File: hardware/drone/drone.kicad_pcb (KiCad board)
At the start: 6 copper layers, 45 x 45 mm, 246 parts, among them J1 54548-2272, J2 BM08B-SRSS-TB_LF__SN_, J3 USB_C_Receptacle_USB2.0_16P, J4 Conn_ARM_SWD_TagConnect_TC2030, J5 Conn_01x06_Pin, J6 Conn_01x02_Socket, Q1 ISP650P06NM, SW1 SW_MEC_5E, U1 STM32N645I0, U10 PE4259, U11 TAC5111IRGER, U12 LP5907, U14 ICM-42688-P, U15 SAM_M10Q, U16 LMR51635XFDDCR, U17 TXU0204, U18 TPS2121, U19 BMP581, U2 SX1262IMLTRT, U20 TVS0500DRV, U21 TCA9406DC, U22 LIS2MDL, U23 MM8030_2610RJ3, U24 MM8030_2610RJ3, U25 ECMF2-40A100N6, U26 ECMF2-40A100N6, U27 ECMF2-40A100N6, U28 LM4670ITL/NOPB, U3 TPS628303, U4 TPS7A2118PQWDSGRQ1, U5 TPS628303, U6 MX25UW25645GXDI00, U7 CC3350, U8 DPX167125DT-8197B1, U9 DEA162450BT-1295A1, Y1 Crystal_GND24, Y2 Crystal_GND24, Y3 Crystal_GND24, Y4 Crystal

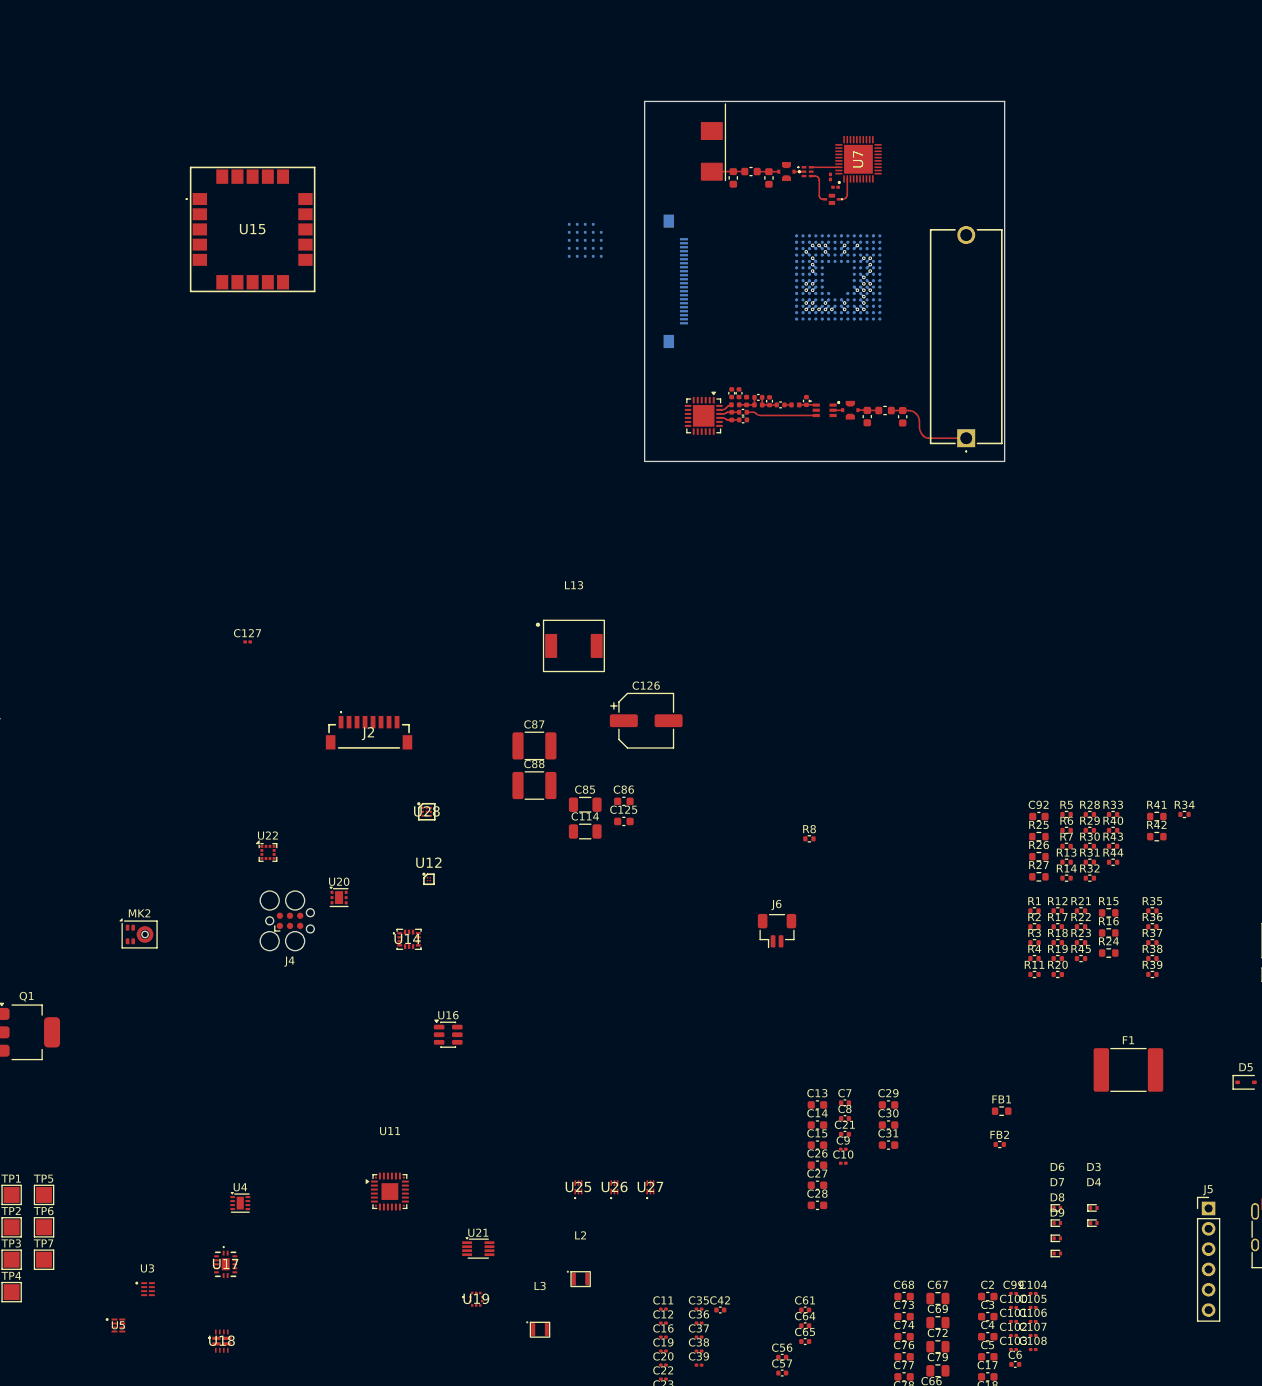
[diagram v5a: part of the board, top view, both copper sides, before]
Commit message: Placed SMPS layouts and optimized for space
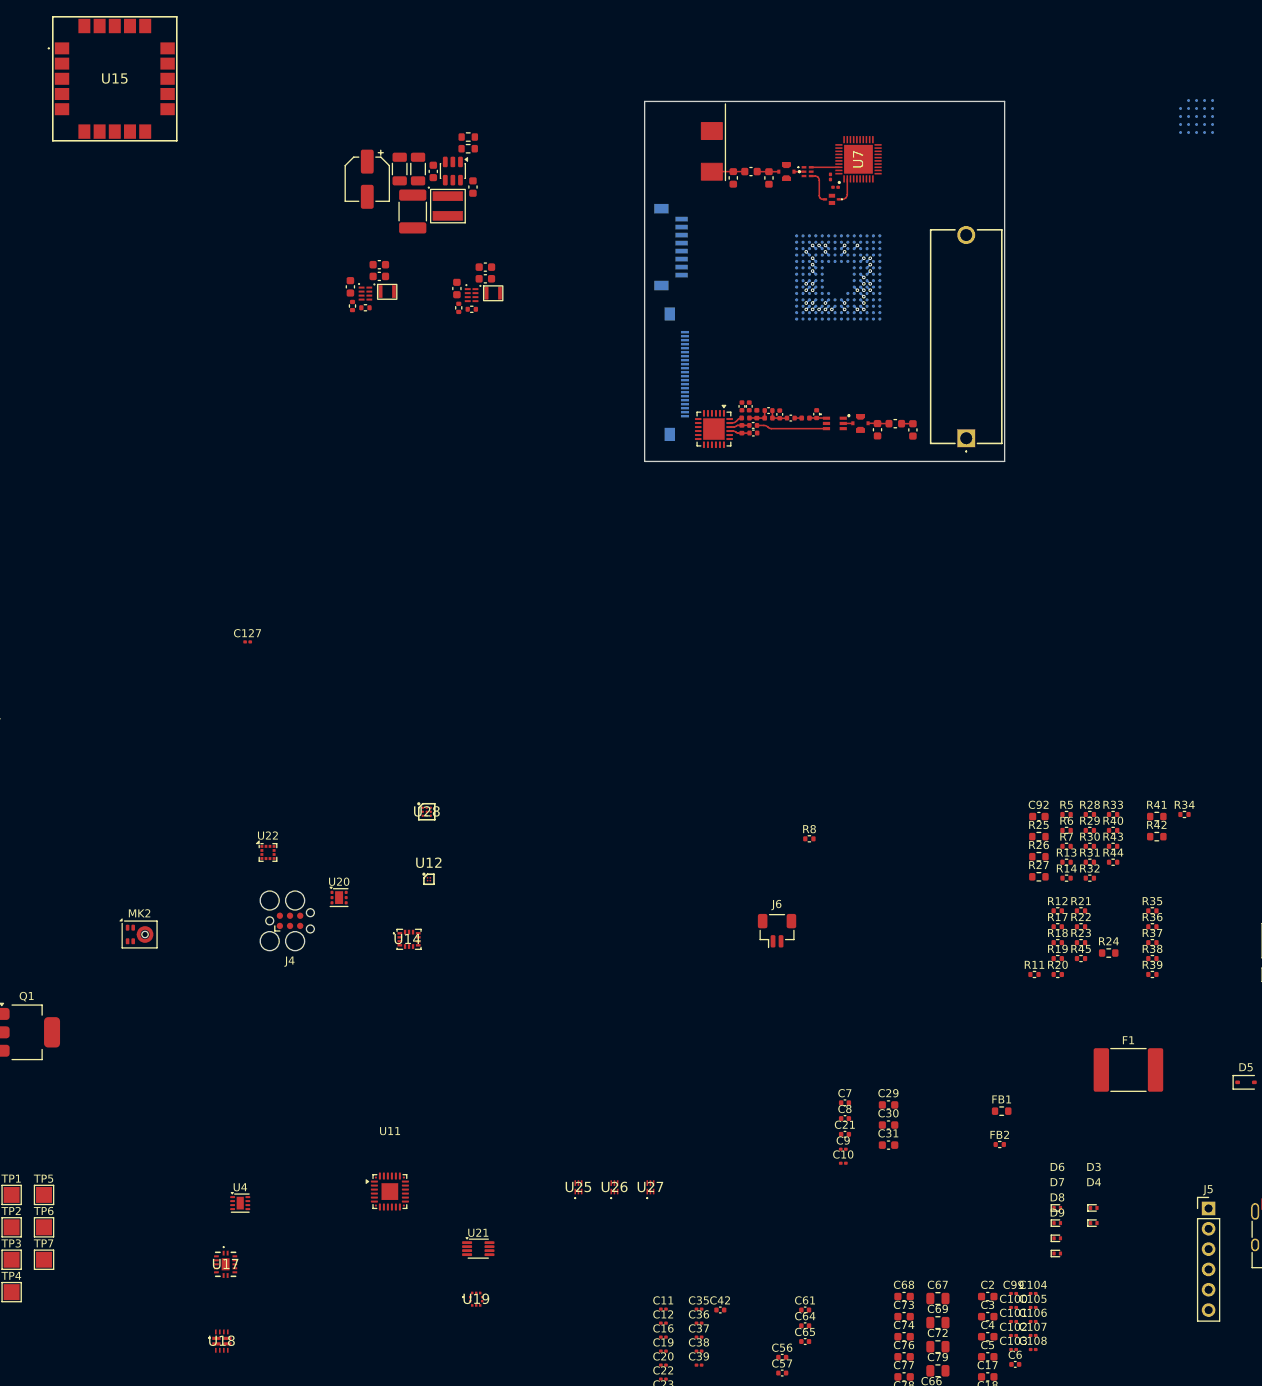
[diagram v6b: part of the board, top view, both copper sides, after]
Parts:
- removed C87: 33u, Capacitor_SMD:C_1812_4532Metric
- C126: value 22u -> 10u; footprint Capacitor_SMD:CP_Elec_6.3x5.4 -> Capacitor_SMD:CP_Elec_5x5.4
- J2: moved to B.Cu
- L13: value 10u -> 3.3u; footprint SoftDroneLibrary:CYA0650-10UH -> SoftDroneLibrary:74439324033
- U16: value LMR51635XFDDCR -> LMR51635YFDDCR
- moved U5 136.2 mm to (149.4, 111.2)
- moved L3 129.7 mm to (152.1, 111.0)
- moved U3 127.4 mm to (136.1, 111.0)
- moved R16 126.6 mm to (148.9, 92.9)
- moved R15 125.8 mm to (148.9, 91.5), turned to 180 degrees
- moved L2 125.8 mm to (138.8, 110.8)
- moved C28 124.4 mm to (151.1, 107.7), turned to 180 degrees
- moved C15 121.6 mm to (137.8, 108.9), turned to 180 degrees
- moved C14 120.7 mm to (137.8, 107.4), turned to 180 degrees
- moved C27 120.7 mm to (151.1, 109.2), turned to 180 degrees
- moved C26 118.5 mm to (147.5, 110.4), turned to -90 degrees
- moved C13 117.8 mm to (134.2, 110.2), turned to -90 degrees
- moved R2 115.3 mm to (134.5, 112.6), turned to 90 degrees
- moved R1 112.6 mm to (136.1, 112.8), turned to 180 degrees
- moved R4 108.6 mm to (147.8, 112.8), turned to 90 degrees
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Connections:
- net Net-(U16-CB) renamed /Power/VSYS_5V_CB
- net Net-(U3-PG) renamed /Power/VDD1V8_PG
- net Net-(U5-PG) renamed /Power/VDD3V3_PG
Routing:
- net /RF_915/RFCSUBG_ANT: track 11.6 -> 1.42 mm

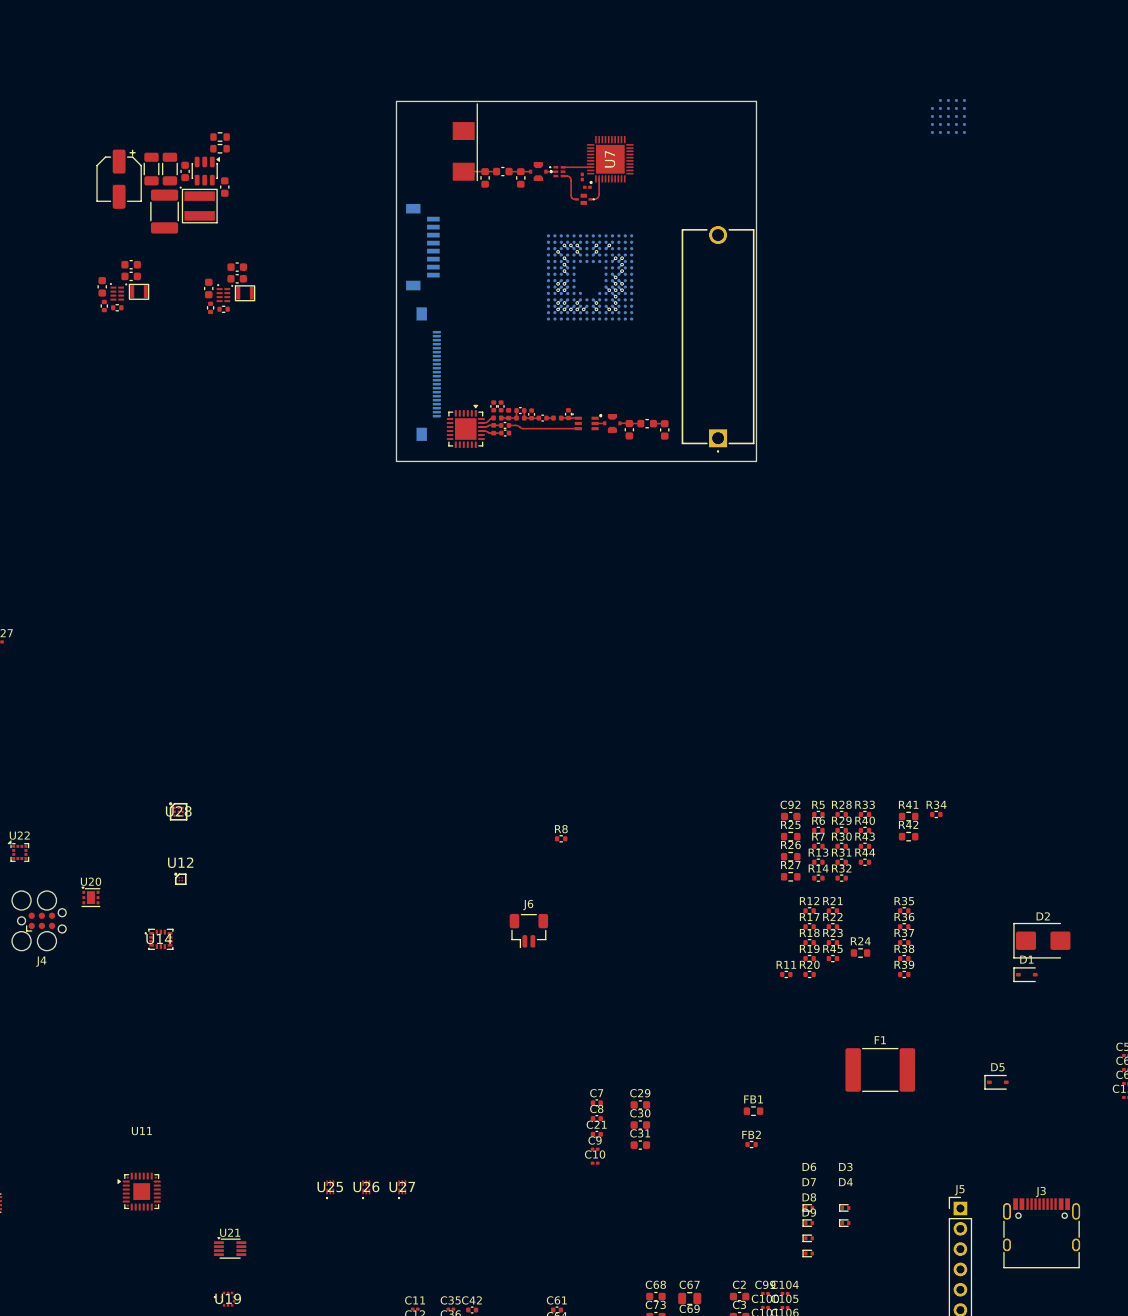
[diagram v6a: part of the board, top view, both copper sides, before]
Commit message: Fixed 3D model of antenna
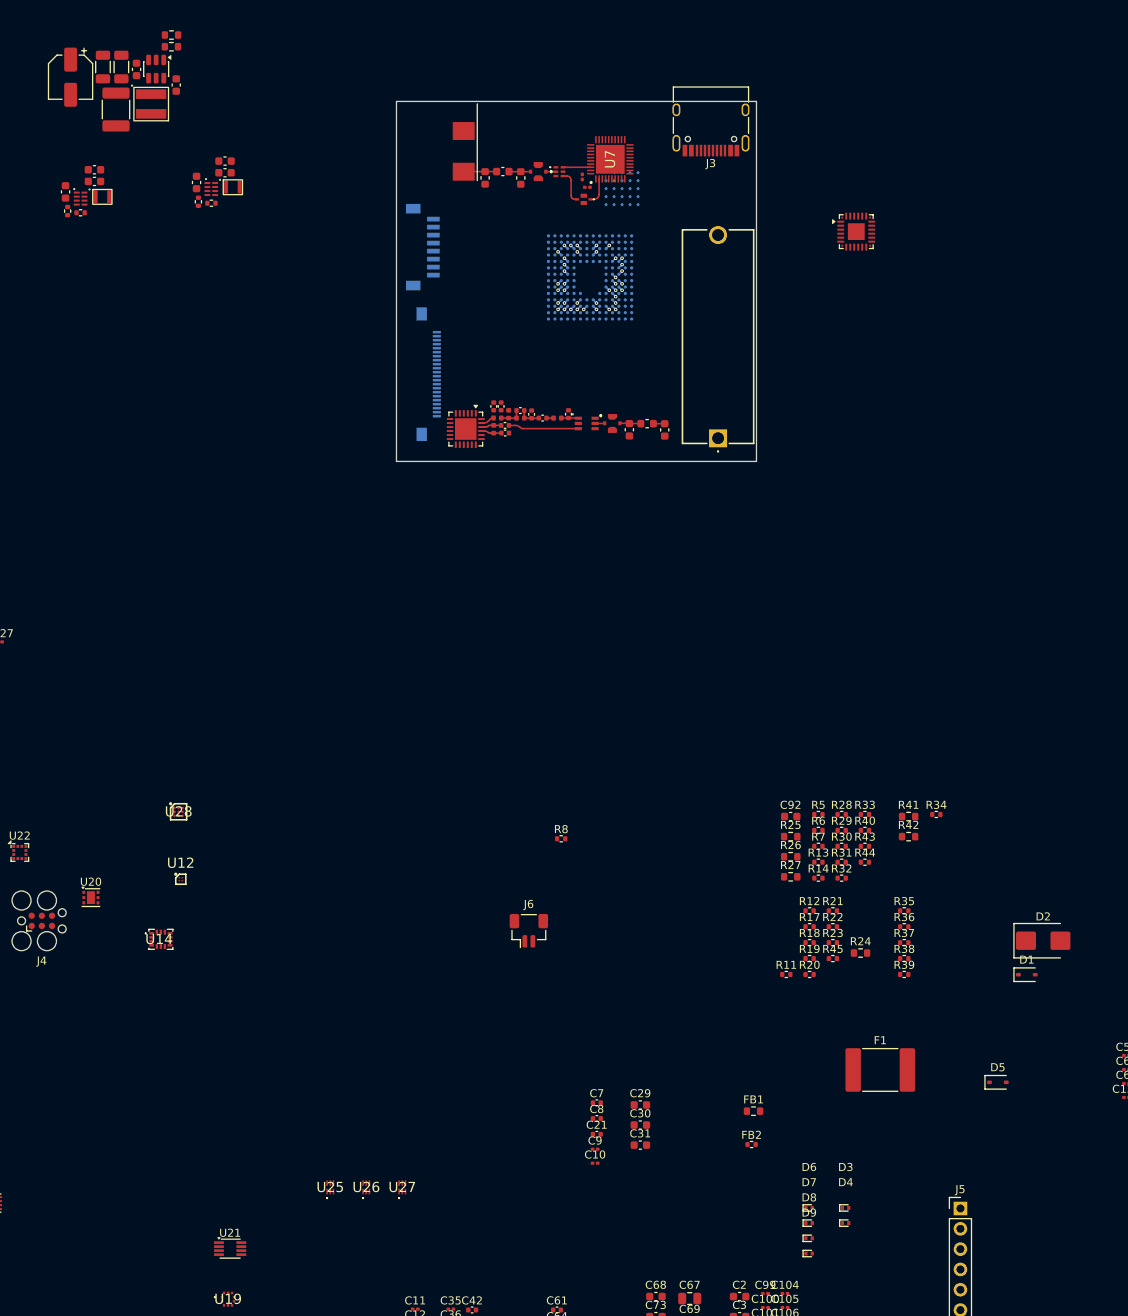
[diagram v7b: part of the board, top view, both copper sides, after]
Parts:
- moved U11 149.6 mm to (228.5, 103.2)
- moved J3 145.8 mm to (210.3, 89.1), turned to 180 degrees
- moved U6 41.8 mm to (199.2, 97.9)
- moved C125 14.1 mm to (138.5, 83.0)
- moved C126 14.1 mm to (130.3, 84.0)
- moved C114 14.1 mm to (136.6, 82.7)
- moved C85 14.1 mm to (134.3, 82.7)
- moved C86 14.1 mm to (143.5, 85.0)
- moved C88 14.1 mm to (135.9, 88.0)
- moved L13 14.1 mm to (140.3, 87.3)
- moved R15 14.1 mm to (142.9, 78.7)
- moved R16 14.1 mm to (142.9, 80.2)
- moved U16 14.1 mm to (141.0, 83.0)
- moved C26 13.3 mm to (146.0, 97.1)
- moved R3 13.3 mm to (147.9, 99.7)
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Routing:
- added copper zone on In1.Cu, net GND
- added copper zone on In4.Cu, net GND

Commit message: Routed OSPI
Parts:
- removed C126: 10u, Capacitor_SMD:CP_Elec_5x5.4
- removed Q1: ISP650P06NM, Package_TO_SOT_SMD:SOT-223
- added U13: SQA411CEJW-T1_GE3, SQA411CEJW-T1_GE3:SQA411CEJWT1_GE3, B.Cu at (203.2, 95.5)
- C114, C125, C13, C14, C15, C26, C27, C28, C29, C30, C31, C32, C33, C34, C85, C86, C88, D1, J3, L13, L2, L3, R1, R15, R16, R2, R3, R4, U11, U16, U18, U3, U5: moved to B.Cu
- F1: value 2920L150/60MR -> SF-0603SP200R-2; footprint Fuse:Fuse_2920_7451Metric -> Fuse:Fuse_0603_1608Metric; moved to B.Cu
- J1, U6: moved to F.Cu
- U25, U26, U27: footprint ECMF2-40A100N6:ECMF240A100N6 -> SoftDroneLibrary:ECMF2-40A100N6
- moved U18 183.5 mm to (219.6, 89.0), turned to 90 degrees
- moved C34 144.7 mm to (195.2, 109.5), turned to 180 degrees
- moved C33 138.8 mm to (196.0, 113.5)
- moved C32 138.8 mm to (199.5, 111.9), turned to -90 degrees
- moved U25 132.0 mm to (196.8, 95.2), turned to 180 degrees
- moved U26 131.8 mm to (200.6, 95.2), turned to 180 degrees
- moved U27 130.4 mm to (198.7, 95.2), turned to 180 degrees
- moved F1 118.9 mm to (200.9, 93.1)
- moved D1 111.7 mm to (201.2, 95.5), turned to -90 degrees
- moved C31 109.4 mm to (195.2, 108.3), turned to 180 degrees
- moved C29 100.6 mm to (200.7, 111.9), turned to -90 degrees
- moved C30 100.4 mm to (196.0, 114.7)
- moved C26 83.4 mm to (229.2, 103.3)
- moved R4 82.9 mm to (228.9, 105.7)
- moved U5 79.7 mm to (227.3, 104.1), turned to 180 degrees
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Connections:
- net /Camera/CSI_CKN_CON renamed /Camera/CSI_CON_CKN
- net /Camera/CSI_CKP_CON renamed /Camera/CSI_CON_CKP
- net /Camera/CSI_D0N_CON renamed /Camera/CSI_CON_D0N
- net /Camera/CSI_D0P_CON renamed /Camera/CSI_CON_D0P
- net /Camera/CSI_D1N_CON renamed /Camera/CSI_CON_D1N
- net /Camera/CSI_D1P_CON renamed /Camera/CSI_CON_D1P
- net Net-(U2-DCC_SW) renamed /RF_915/SX_DCC_SW
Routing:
- net /Camera/CSI_D1N: track 0.00 -> 29.1 mm, vias 0 -> 1
- net /Camera/CSI_D0N: track 0.00 -> 28.7 mm, vias 0 -> 1
- net /Camera/CSI_D1P: track 0.00 -> 28.1 mm, vias 0 -> 1
- net /Camera/CSI_D0P: track 0.00 -> 27.7 mm, vias 0 -> 1
- net /Camera/CSI_CKN: track 0.00 -> 26.9 mm, vias 0 -> 1
- net /Camera/CSI_CKP: track 0.00 -> 25.9 mm, vias 0 -> 1
- net /MCU/OSPI_IO0: track 0.00 -> 14.3 mm, vias 0 -> 1
- net /MCU/OSPI_DQS: track 0.00 -> 12.7 mm, vias 0 -> 1
- net /MCU/OSPI_IO1: track 0.00 -> 12.5 mm, vias 0 -> 1
- net /MCU/OSPI_CLK: track 0.57 -> 11.1 mm
- net /MCU/OSPI_IO7: track 0.00 -> 9.69 mm, vias 0 -> 1
- net /MCU/OSPI_IO5: track 0.00 -> 9.35 mm, vias 0 -> 1
- net /MCU/OSPI_IO4: track 0.00 -> 8.23 mm, vias 0 -> 1
- net /MCU/OSPI_IO6: track 0.00 -> 8.06 mm, vias 0 -> 1
- net /MCU/OSPI_IO2: track 0.00 -> 8.04 mm, vias 0 -> 1
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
